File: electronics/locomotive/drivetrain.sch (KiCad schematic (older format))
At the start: 8 parts

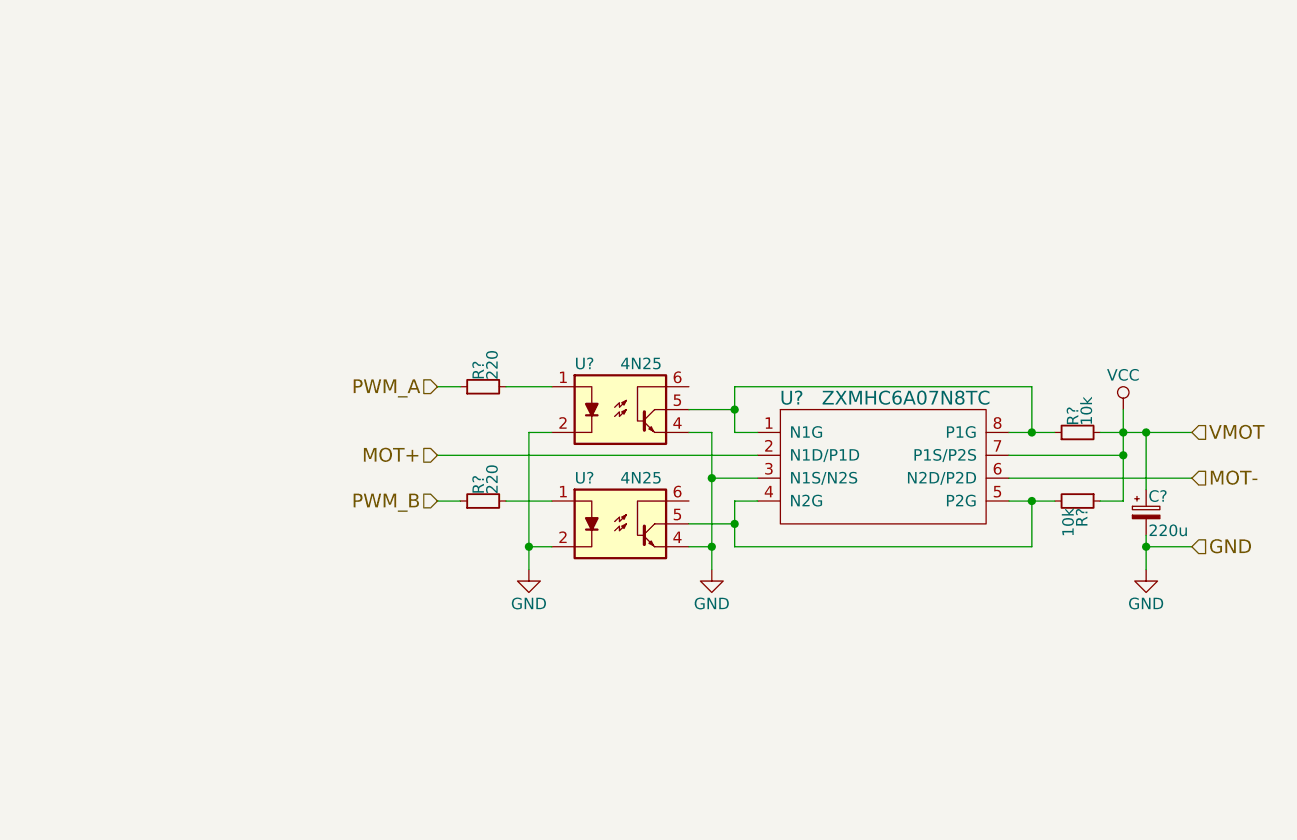
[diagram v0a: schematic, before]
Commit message: electronics: locomotive: Update schematics
Voltage regulator, TOF, IR receiver, voltage scaler, I2C control lines, power
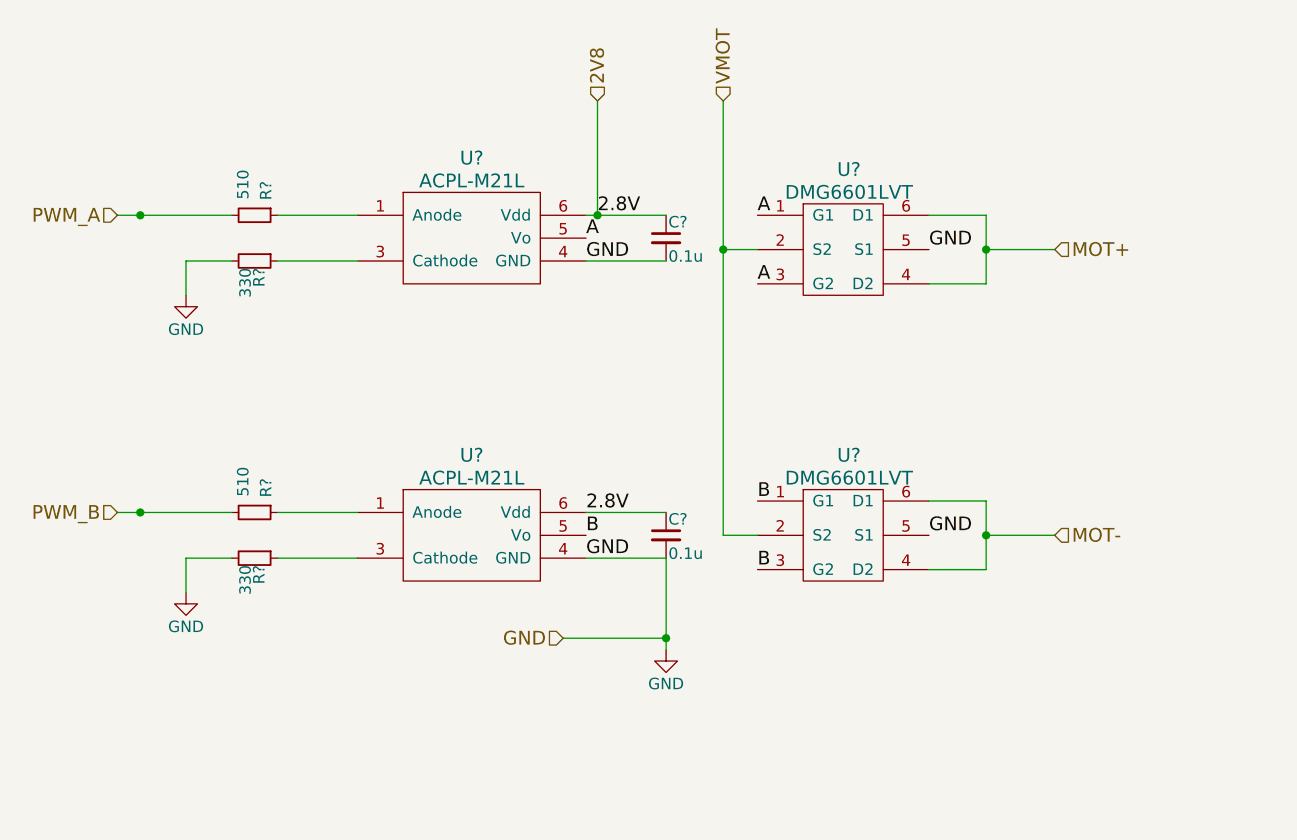
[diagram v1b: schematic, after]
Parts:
- removed C?: 220u, symbol CP_Small
- removed R? (x2): 10k, symbol R_Small
- removed R? (x2): 220, symbol R_Small
- removed U?: ZXMHC6A07N8TC, symbol ZXMHC6A07N8TC
- removed U? (x2): 4N25, DIP-6, symbol 4N25
- added C? (x2): 0.1u, symbol C_Small
- added R? (x2): 510, symbol R_Small
- added R? (x2): 330, symbol R_Small
- added U? (x2): DMG6601LVT, symbol DMG6601LVT
- added U? (x2): ACPL-M21L, symbol ACPL-M21L
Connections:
- net GND: now also C?.2, C?.2, R?.2, R?.2, U?.4 (GND), U?.4 (GND), U?.5 (S1), U?.5 (S1)
- net MOT+: now also U?.4 (D2), U?.6 (D1)
- net MOT-: now also U?.4 (D2), U?.6 (D1)
- net PWM_A: now also R?.2
- net PWM_B: now also R?.2
- new net: R?.1, U?.1 (Anode) (x2)
- new net: R?.1, U?.3 (Cathode) (x2)
- new net 2V8: C?.1, C?.1, U?.6 (Vdd), U?.6 (Vdd)
- new net A: U?.1 (G1), U?.3 (G2), U?.5 (Vo)
- new net B: U?.1 (G1), U?.3 (G2), U?.5 (Vo)
- new net VMOT: U?.2 (S2), U?.2 (S2)

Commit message: firmware: locomotive: Change voltage regulator resistor values
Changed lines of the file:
@@
 	4600 2450 4600 2950
 Wire Wire Line
-	4550 2950 4600 2950
-Wire Wire Line
-	4600 2950 4900 2950
+	4550 2950 4900 2950
 Connection ~ 4600 2950
 Wire Wire Line
@@
 	3200 4450 3550 4450
 Wire Wire Line
-	2500 4250 2600 4250
+	2500 4250 3000 4250
 Wire Wire Line
-	2600 4250 3000 4250
-Wire Wire Line
-	2500 2950 2600 2950
-Wire Wire Line
-	2600 2950 3000 2950
+	2500 2950 3000 2950
 Connection ~ 2600 2950
 Connection ~ 2600 4250
@@
 B
 Wire Wire Line
-	4900 4450 4900 4800
-Wire Wire Line
-	4900 4800 4900 4850
+	4900 4450 4900 4850
 Connection ~ 4900 4800
 Wire Wire Line
-	5150 2450 5150 3100
-Wire Wire Line
-	5150 3100 5150 4350
+	5150 2450 5150 4350
 Wire Wire Line
 	5150 3100 5300 3100
@@
 Connection ~ 5150 3100
 Wire Wire Line
-	6050 4500 6300 4500
+	6300 4500 6050 4500
 Wire Wire Line
-	6300 4500 6300 4350
-Wire Wire Line
-	6300 4350 6300 4200
+	6300 4200 6300 4500
 Wire Wire Line
 	6300 4200 6050 4200
 Wire Wire Line
-	6050 3250 6300 3250
+	6300 3250 6050 3250
 Wire Wire Line
-	6300 3250 6300 3100
-Wire Wire Line
-	6300 3100 6300 2950
+	6300 2950 6300 3250
 Wire Wire Line
 	6300 2950 6050 2950

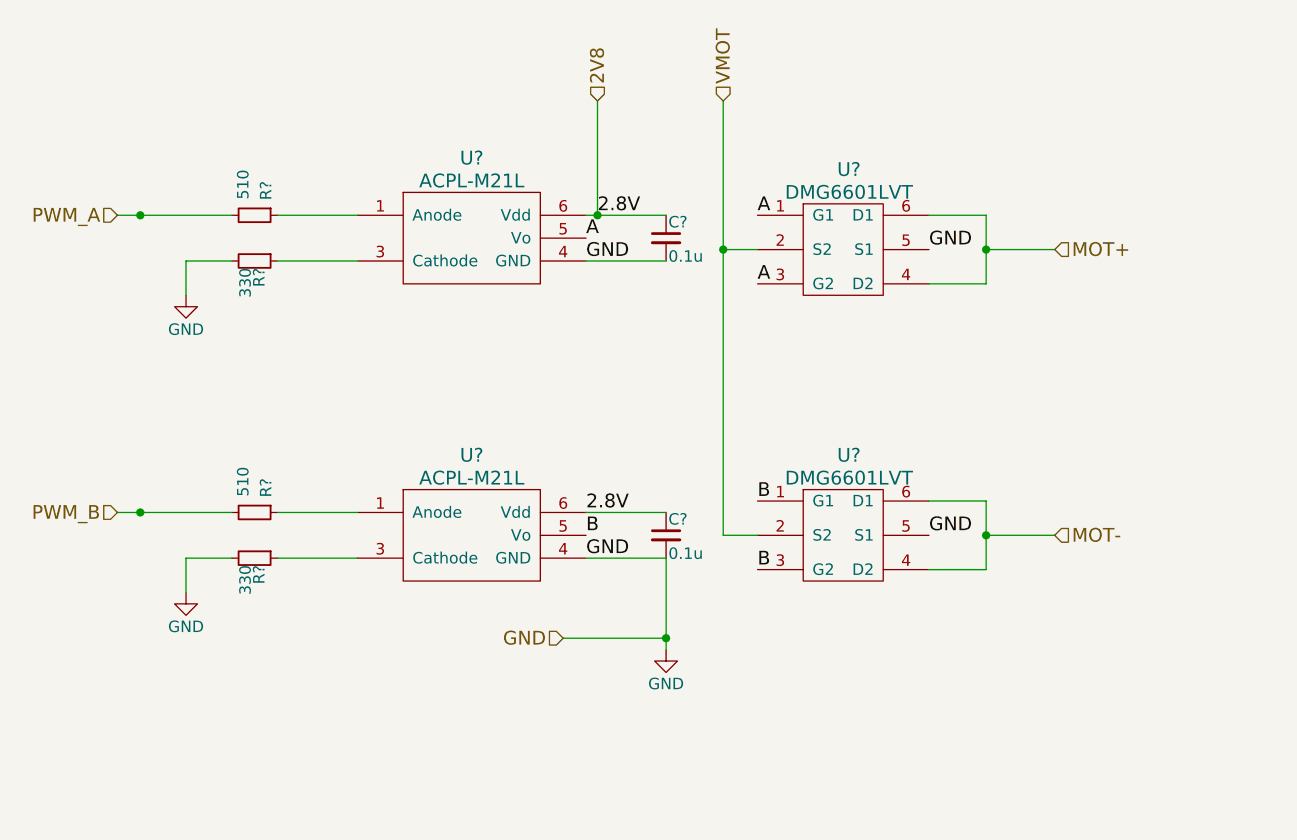
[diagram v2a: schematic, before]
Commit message: electronics: locomotive: Fix up schematics
- add all parts and label them
- some values still tentative
- still need to finish connectors
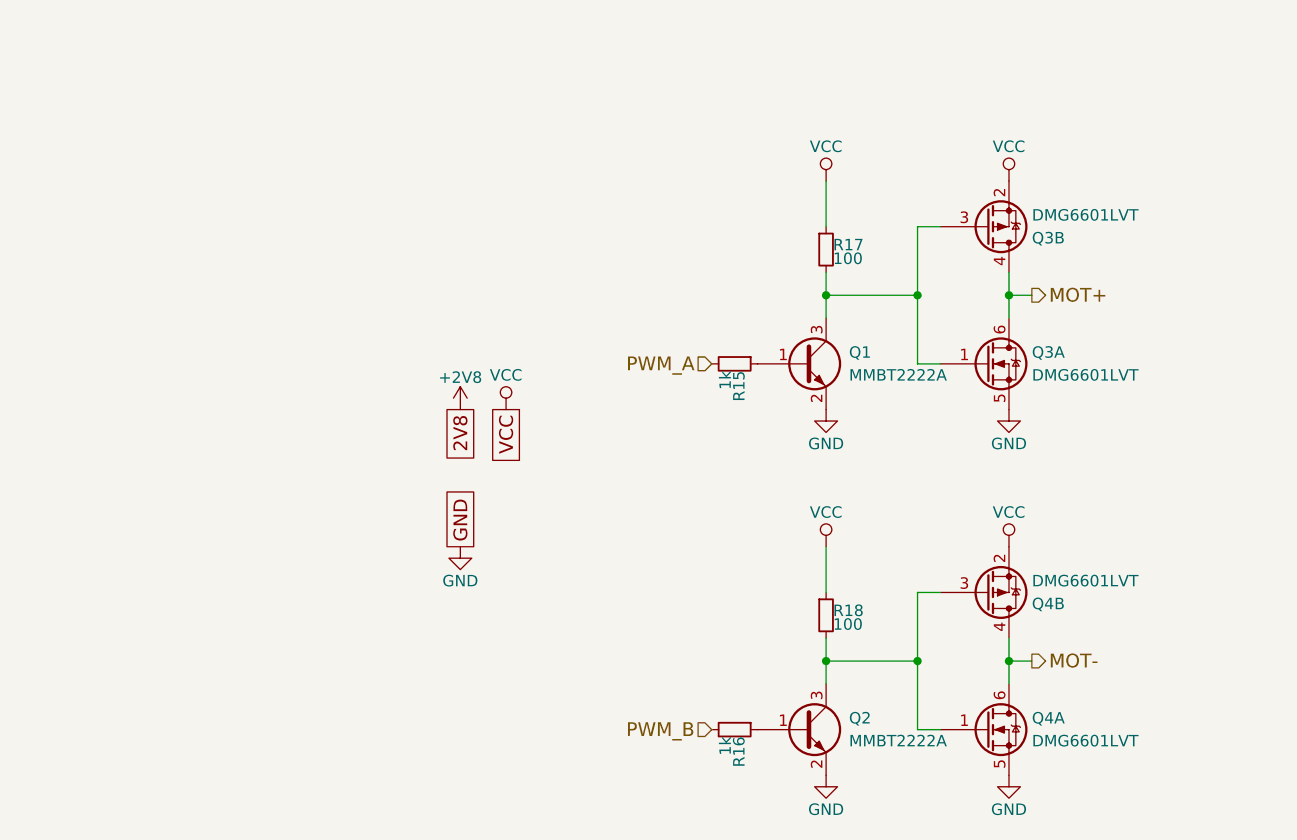
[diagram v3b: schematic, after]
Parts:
- removed C? (x2): 0.1u, symbol C_Small
- removed R? (x2): 510, symbol R_Small
- removed R? (x2): 330, symbol R_Small
- removed U? (x2): DMG6601LVT, symbol DMG6601LVT
- removed U? (x2): ACPL-M21L, symbol ACPL-M21L
- added Q1, Q2: MMBT2222A, symbol Q_NPN_BEC
- added Q3, Q4: DMG6601LVT, symbol Q_DUAL_NMOS_PMOS_G1S2G2D2S1D1
- added R15, R16: 1k, symbol R_Small
- added R17, R18: 100, symbol R_Small
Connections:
- net GND: now also Q1.2 (E), Q2.2 (E), Q3.5 (S), Q4.5 (S)
- net MOT+: now also Q3.4 (D), Q3.6 (D)
- net MOT-: now also Q4.4 (D), Q4.6 (D)
- net PWM_A: now also R15.2
- net PWM_B: now also R16.2
- new net: Q1.1 (B), R15.1
- new net: Q1.3 (C), Q3.1 (G), Q3.3 (G), R17.2
- new net: Q2.1 (B), R16.1
- new net: Q2.3 (C), Q4.1 (G), Q4.3 (G), R18.2
- new net VCC: Q3.2 (S), Q4.2 (S), R17.1, R18.1

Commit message: electronics: locomotive: Board Rev 1.0
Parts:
- Q1, Q2: footprint (none) -> TO_SOT_Packages_SMD:SOT-23
- Q3, Q4: footprint (none) -> TO_SOT_Packages_SMD:SOT-23-6
- R15, R16: footprint (none) -> Resistors_SMD:R_0603
- R17, R18: footprint (none) -> Resistors_SMD:R_2512
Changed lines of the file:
@@
 $Descr A4 11693 8268
 encoding utf-8
-Sheet 4 5
+Sheet 3 4
 Title ""
 Date ""
@@
 PWM_B
 $Comp
-L GND #PWR043
+L GND #PWR033
 U 1 1 58C48F9D
 P 5600 5400
-F 0 "#PWR043" H 5600 5150 50  0001 C CNN
+F 0 "#PWR033" H 5600 5150 50  0001 C CNN
 F 1 "GND" H 5600 5250 50  0000 C CNN
 F 2 "" H 5600 5400 50  0001 C CNN
@@
 $EndComp
 $Comp
-L +2V8 #PWR044
-U 1 1 58D2850D
-P 4000 3800
-F 0 "#PWR044" H 4000 3650 50  0001 C CNN
-F 1 "+2V8" H 4000 3940 50  0000 C CNN
-F 2 "" H 4000 3800 50  0001 C CNN
-F 3 "" H 4000 3800 50  0001 C CNN
-	1    4000 3800
-	1    0    0    -1
-$EndComp
-$Comp
-L GND #PWR045
+L GND #PWR034
 U 1 1 58D28513
 P 4000 4400
-F 0 "#PWR045" H 4000 4150 50  0001 C CNN
+F 0 "#PWR034" H 4000 4150 50  0001 C CNN
 F 1 "GND" H 4000 4250 50  0000 C CNN
 F 2 "" H 4000 4400 50  0001 C CNN
@@
 $EndComp
 $Comp
-L VCC #PWR046
+L VCC #PWR035
 U 1 1 58D2882F
 P 6400 2800
-F 0 "#PWR046" H 6400 2650 50  0001 C CNN
+F 0 "#PWR035" H 6400 2650 50  0001 C CNN
 F 1 "VCC" H 6400 2950 50  0000 C CNN
 F 2 "" H 6400 2800 50  0001 C CNN
@@
 $EndComp
 $Comp
-L VCC #PWR047
+L VCC #PWR036
 U 1 1 58D2885F
-P 4200 3800
-F 0 "#PWR047" H 4200 3650 50  0001 C CNN
-F 1 "VCC" H 4200 3950 50  0000 C CNN
-F 2 "" H 4200 3800 50  0001 C CNN
-F 3 "" H 4200 3800 50  0001 C CNN
-	1    4200 3800
+P 4000 3800
+F 0 "#PWR036" H 4000 3650 50  0001 C CNN
+F 1 "VCC" H 4000 3950 50  0000 C CNN
+F 2 "" H 4000 3800 50  0001 C CNN
+F 3 "" H 4000 3800 50  0001 C CNN
+	1    4000 3800
 	1    0    0    -1
 $EndComp
@@
 F 0 "Q3" H 6500 3650 50  0000 L CNN
 F 1 "DMG6601LVT" H 6500 3550 50  0000 L CNN
-F 2 "" H 6500 3700 50  0001 C CNN
+F 2 "TO_SOT_Packages_SMD:SOT-23-6" H 6500 3700 50  0001 C CNN
 F 3 "" H 6300 3600 50  0001 C CNN
 	1    6300 3600
@@
 F 0 "Q3" H 6500 3050 50  0000 L CNN
 F 1 "DMG6601LVT" H 6500 2950 50  0000 L CNN
-F 2 "" H 6500 3100 50  0001 C CNN
+F 2 "TO_SOT_Packages_SMD:SOT-23-6" H 6500 3100 50  0001 C CNN
 F 3 "" H 6300 3000 50  0001 C CNN
 	2    6300 3000
@@
 $EndComp
 $Comp
-L GND #PWR048
+L GND #PWR037
 U 1 1 58D269B3
 P 6400 5400
-F 0 "#PWR048" H 6400 5150 50  0001 C CNN
+F 0 "#PWR037" H 6400 5150 50  0001 C CNN
 F 1 "GND" H 6400 5250 50  0000 C CNN
 F 2 "" H 6400 5400 50  0001 C CNN
@@
 F 0 "Q4" H 6500 5250 50  0000 L CNN
 F 1 "DMG6601LVT" H 6500 5150 50  0000 L CNN
-F 2 "" H 6500 5300 50  0001 C CNN
+F 2 "TO_SOT_Packages_SMD:SOT-23-6" H 6500 5300 50  0001 C CNN
 F 3 "" H 6300 5200 50  0001 C CNN
 	1    6300 5200
@@
 F 0 "Q4" H 6500 4650 50  0000 L CNN
 F 1 "DMG6601LVT" H 6500 4550 50  0000 L CNN
-F 2 "" H 6500 4700 50  0001 C CNN
+F 2 "TO_SOT_Packages_SMD:SOT-23-6" H 6500 4700 50  0001 C CNN
 F 3 "" H 6300 4600 50  0001 C CNN
 	2    6300 4600
@@
 Connection ~ 6400 4900
 $Comp
-L GND #PWR049
+L GND #PWR038
 U 1 1 58D6CB4C
 P 5600 3800
-F 0 "#PWR049" H 5600 3550 50  0001 C CNN
+F 0 "#PWR038" H 5600 3550 50  0001 C CNN
 F 1 "GND" H 5600 3650 50  0000 C CNN
 F 2 "" H 5600 3800 50  0001 C CNN
@@
 $EndComp
 $Comp
-L GND #PWR050
+L GND #PWR039
 U 1 1 58D6D1FC
 P 6400 3800
-F 0 "#PWR050" H 6400 3550 50  0001 C CNN
+F 0 "#PWR039" H 6400 3550 50  0001 C CNN
 F 1 "GND" H 6400 3650 50  0000 C CNN
 F 2 "" H 6400 3800 50  0001 C CNN
@@
 $EndComp
 $Comp
-L VCC #PWR051
+L VCC #PWR040
 U 1 1 58D6D3AF
 P 6400 4400
-F 0 "#PWR051" H 6400 4250 50  0001 C CNN
+F 0 "#PWR040" H 6400 4250 50  0001 C CNN
 F 1 "VCC" H 6400 4550 50  0000 C CNN
 F 2 "" H 6400 4400 50  0001 C CNN
@@
 GND
 Text GLabel 4000 3800 3    60   UnSpc ~ 0
-2V8
-Text GLabel 4200 3800 3    60   UnSpc ~ 0
 VCC
 $Comp
@@
 F 0 "Q1" H 5700 3650 50  0000 L CNN
 F 1 "MMBT2222A" H 5700 3550 50  0000 L CNN
-F 2 "" H 5700 3700 50  0001 C CNN
+F 2 "TO_SOT_Packages_SMD:SOT-23" H 5700 3700 50  0001 C CNN
 F 3 "" H 5500 3600 50  0001 C CNN
 	1    5500 3600
@@
 $EndComp
 $Comp
-L VCC #PWR052
+L VCC #PWR041
 U 1 1 58D39FD1
 P 5600 2800
-F 0 "#PWR052" H 5600 2650 50  0001 C CNN
+F 0 "#PWR041" H 5600 2650 50  0001 C CNN
 F 1 "VCC" H 5600 2950 50  0000 C CNN
 F 2 "" H 5600 2800 50  0001 C CNN
@@
 $EndComp
 $Comp
-L VCC #PWR053
+L VCC #PWR042
 U 1 1 58D3A062
 P 5600 4400
-F 0 "#PWR053" H 5600 4250 50  0001 C CNN
+F 0 "#PWR042" H 5600 4250 50  0001 C CNN
 F 1 "VCC" H 5600 4550 50  0000 C CNN
 F 2 "" H 5600 4400 50  0001 C CNN
@@
 F 0 "Q2" H 5700 5250 50  0000 L CNN
 F 1 "MMBT2222A" H 5700 5150 50  0000 L CNN
-F 2 "" H 5700 5300 50  0001 C CNN
+F 2 "TO_SOT_Packages_SMD:SOT-23" H 5700 5300 50  0001 C CNN
 F 3 "" H 5500 5200 50  0001 C CNN
 	1    5500 5200
@@
 F 0 "R17" H 5630 3120 50  0000 L CNN
 F 1 "100" H 5630 3060 50  0000 L CNN
-F 2 "" H 5600 3100 50  0001 C CNN
+F 2 "Resistors_SMD:R_2512" H 5600 3100 50  0001 C CNN
 F 3 "" H 5600 3100 50  0001 C CNN
 	1    5600 3100
@@
 F 0 "R18" H 5630 4720 50  0000 L CNN
 F 1 "100" H 5630 4660 50  0000 L CNN
-F 2 "" H 5600 4700 50  0001 C CNN
+F 2 "Resistors_SMD:R_2512" H 5600 4700 50  0001 C CNN
 F 3 "" H 5600 4700 50  0001 C CNN
 	1    5600 4700
@@
 F 0 "R15" H 5230 3620 50  0000 L CNN
 F 1 "1k" H 5230 3560 50  0000 L CNN
-F 2 "" H 5200 3600 50  0001 C CNN
+F 2 "Resistors_SMD:R_0603" H 5200 3600 50  0001 C CNN
 F 3 "" H 5200 3600 50  0001 C CNN
 	1    5200 3600
@@
 F 0 "R16" H 5230 5220 50  0000 L CNN
 F 1 "1k" H 5230 5160 50  0000 L CNN
-F 2 "" H 5200 5200 50  0001 C CNN
+F 2 "Resistors_SMD:R_0603" H 5200 5200 50  0001 C CNN
 F 3 "" H 5200 5200 50  0001 C CNN
 	1    5200 5200
